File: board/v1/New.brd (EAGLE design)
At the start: 21.8 x 22.6 mm, 28 parts, among them IC2 LTC3525, IC3 MCP1703CB, U3 ATMEGA32U4, X1 USB-MICROB, Y1 16MHz

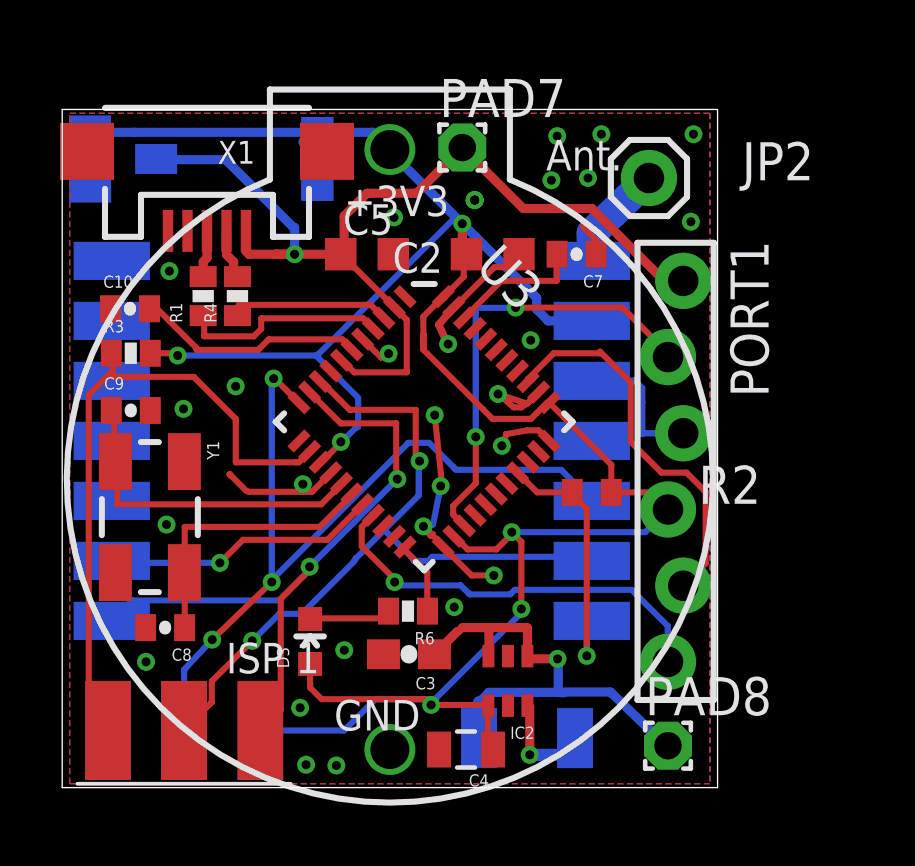
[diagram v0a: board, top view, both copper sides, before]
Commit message: some clearance fix
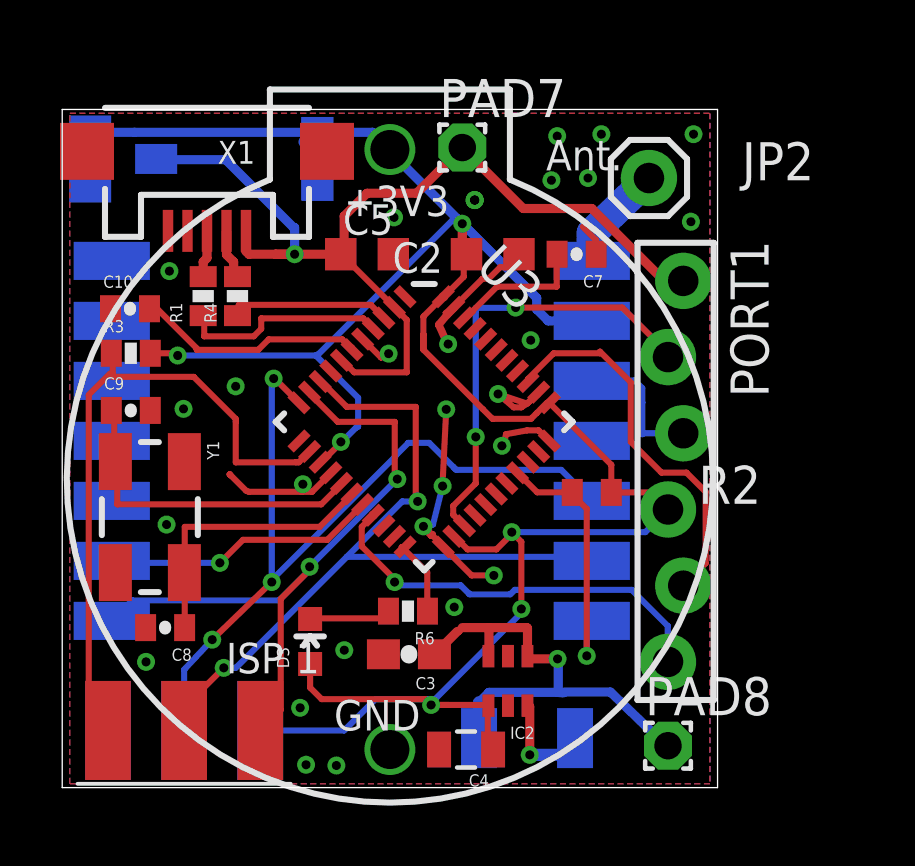
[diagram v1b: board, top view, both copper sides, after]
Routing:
- net SCK: track 25.6 -> 26.7 mm
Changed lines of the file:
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@@
 <autorouter>
 <pass name="Default">
-<param name="RoutingGrid" value="0.05mm"/>
+<param name="RoutingGrid" value="0.1mm"/>
 <param name="tpViaShape" value="round"/>
 <param name="PrefDir.1" value="|"/>
@@
 <wire x1="11.648" y1="14.848" x2="11.640103125" y2="14.848" width="0.2032" layer="1"/>
 <wire x1="11.640103125" y1="14.848" x2="11.0303875" y2="15.457715625" width="0.2032" layer="1"/>
-<via x="13.432" y="12.925" extent="1-16" drill="0.3"/>
+<via x="13.816" y="13.117" extent="1-16" drill="0.3"/>
 <wire x1="18.811" y1="18.288" x2="18.811" y2="18.757" width="0.2032" layer="1"/>
 <wire x1="18.811" y1="18.757" x2="18.368" y2="19.2" width="0.2032" layer="1"/>
 <wire x1="14.070946875" y1="16.518375" x2="14.086375" y2="16.518375" width="0.2032" layer="1"/>
-<wire x1="14.086375" y1="16.518375" x2="15.424" y2="17.856" width="0.2032" layer="1"/>
-<wire x1="15.424" y1="17.856" x2="15.81" y2="17.856" width="0.2032" layer="1"/>
 <wire x1="15.81" y1="17.856" x2="16.242" y2="18.288" width="0.2032" layer="1"/>
 <via x="14.764" y="20.093" extent="1-16" drill="0.3"/>
@@
 <wire x1="15.403" y1="7.581" x2="14.6644625" y2="7.581" width="0.2032" layer="1"/>
 <wire x1="14.6644625" y1="7.581" x2="13.71739375" y2="8.52806875" width="0.2032" layer="1"/>
-<wire x1="13.432" y1="12.925" x2="13.688" y2="10.504" width="0.2032" layer="1"/>
-<wire x1="13.688" y1="10.504" x2="13.632" y2="10.56" width="0.2032" layer="1"/>
-<via x="13.632" y="10.56" extent="1-16" drill="0.3"/>
-<wire x1="13.632" y1="10.56" x2="13.376" y2="9.28" width="0.2032" layer="16"/>
+<wire x1="13.816" y1="13.117" x2="13.688" y2="10.504" width="0.2032" layer="1"/>
+<wire x1="13.688" y1="10.504" x2="13.696" y2="10.56" width="0.2032" layer="1"/>
+<via x="13.696" y="10.56" extent="1-16" drill="0.3"/>
+<wire x1="13.696" y1="10.56" x2="13.376" y2="9.28" width="0.2032" layer="16"/>
 <wire x1="13.376" y1="9.28" x2="13.056" y2="9.216" width="0.2032" layer="16"/>
 <via x="13.056" y="9.216" extent="1-16" drill="0.3"/>
@@
 <wire x1="6.65" y1="10.9" x2="6.599" y2="10.951" width="0.2032" layer="1"/>
 <wire x1="7.15" y1="10.4" x2="7.243" y2="10.368" width="0.2032" layer="1"/>
+<wire x1="14.070946875" y1="16.518375" x2="15.024571875" y2="17.472" width="0.2032" layer="1"/>
+<wire x1="15.024571875" y1="17.472" x2="15.232" y2="17.472" width="0.2032" layer="1"/>
+<wire x1="15.232" y1="17.472" x2="15.616" y2="17.856" width="0.2032" layer="1"/>
+<wire x1="15.616" y1="17.856" x2="15.81" y2="17.856" width="0.2032" layer="1"/>
 </signal>
 <signal name="SCK">
@@
 <contactref element="U$2" pad="SCK"/>
 <contactref element="U3" pad="9"/>
-<wire x1="13.248" y1="8.065" x2="12.736" y2="8.065" width="0.2032" layer="16"/>
 <wire x1="9.616175" y1="14.0435" x2="9.6365" y2="14.0435" width="0.2032" layer="1"/>
-<via x="12.928" y="11.392" extent="1-16" drill="0.3"/>
-<wire x1="12.9" y1="11.35" x2="12.928" y2="11.392" width="0.2032" layer="16"/>
 <wire x1="18.55" y1="8.2" x2="18.65" y2="8.1" width="0.2032" layer="16"/>
-<wire x1="13.35" y1="8.2" x2="18.55" y2="8.2" width="0.2032" layer="16"/>
-<wire x1="13.3" y1="8.15" x2="13.35" y2="8.2" width="0.2032" layer="16"/>
 <wire x1="18.65" y1="8.1" x2="18.668" y2="8.065" width="0.2032" layer="16"/>
-<wire x1="13.3" y1="8.15" x2="13.248" y2="8.065" width="0.2032" layer="16"/>
-<wire x1="12.9" y1="10.25" x2="12.9" y2="11.25" width="0.2032" layer="16"/>
-<wire x1="10.8" y1="8.15" x2="11.75" y2="9.1" width="0.2032" layer="16"/>
-<wire x1="11.75" y1="9.1" x2="12.9" y2="10.25" width="0.2032" layer="16"/>
-<wire x1="12.9" y1="11.25" x2="12.928" y2="11.392" width="0.2032" layer="16"/>
-<wire x1="10.8" y1="8.15" x2="10.753" y2="8.065" width="0.2032" layer="16"/>
-<wire x1="12.7" y1="8.15" x2="11.8" y2="9.05" width="0.2032" layer="16"/>
-<wire x1="11.8" y1="9.05" x2="11.75" y2="9.1" width="0.2032" layer="16"/>
-<wire x1="12.7" y1="8.15" x2="12.736" y2="8.065" width="0.2032" layer="16"/>
-<wire x1="10.6" y1="13.1" x2="9.7" y2="14" width="0.2032" layer="1"/>
-<wire x1="12.8" y1="13.1" x2="10.6" y2="13.1" width="0.2032" layer="1"/>
-<wire x1="12.8" y1="11.5" x2="12.8" y2="13.1" width="0.2032" layer="1"/>
-<wire x1="12.9" y1="11.4" x2="12.8" y2="11.5" width="0.2032" layer="1"/>
+<wire x1="5.1" y1="2.45" x2="5.08" y2="2.413" width="0.2032" layer="1"/>
+<wire x1="5.1" y1="2.5" x2="5.08" y2="2.413" width="0.2032" layer="1"/>
+<wire x1="10.5" y1="8.2" x2="18.5" y2="8.2" width="0.2032" layer="16"/>
+<wire x1="6.8" y1="4.5" x2="10.5" y2="8.2" width="0.2032" layer="16"/>
+<wire x1="6.4" y1="4.5" x2="6.8" y2="4.5" width="0.2032" layer="16"/>
+<wire x1="5.1" y1="3.2" x2="6.4" y2="4.5" width="0.2032" layer="1"/>
+<wire x1="5.1" y1="2.6" x2="5.1" y2="3.2" width="0.2032" layer="1"/>
+<wire x1="18.5" y1="8.2" x2="18.668" y2="8.065" width="0.2032" layer="16"/>
+<wire x1="5.1" y1="2.6" x2="5.08" y2="2.413" width="0.2032" layer="1"/>
+<via x="6.4" y="4.5" extent="1-16" drill="0.3"/>
+<wire x1="10.5" y1="8.2" x2="12.348" y2="10.048" width="0.2032" layer="16"/>
+<wire x1="12.348" y1="10.048" x2="12.864" y2="10.048" width="0.2032" layer="16"/>
+<via x="12.864" y="10.048" extent="1-16" drill="0.3"/>
+<wire x1="9.6" y1="14.1" x2="9.616175" y2="14.0435" width="0.2032" layer="1"/>
+<wire x1="9.6" y1="14.1" x2="9.6" y2="14.08" width="0.2032" layer="1"/>
+<wire x1="10.5" y1="13.2" x2="9.7" y2="14" width="0.2032" layer="1"/>
+<wire x1="12.8" y1="13.2" x2="10.5" y2="13.2" width="0.2032" layer="1"/>
+<wire x1="12.8" y1="10.1" x2="12.8" y2="13.2" width="0.2032" layer="1"/>
 <wire x1="9.7" y1="14" x2="9.616175" y2="14.0435" width="0.2032" layer="1"/>
-<wire x1="12.9" y1="11.4" x2="12.928" y2="11.392" width="0.2032" layer="1"/>
-<wire x1="6" y1="3.35" x2="5.1" y2="2.45" width="0.2032" layer="1"/>
-<wire x1="6" y1="4.05" x2="6" y2="3.35" width="0.2032" layer="1"/>
-<wire x1="7.35" y1="5.4" x2="6" y2="4.05" width="0.2032" layer="1"/>
-<wire x1="8.25" y1="6.3" x2="7.35" y2="5.4" width="0.2032" layer="16"/>
-<wire x1="9" y1="6.3" x2="8.25" y2="6.3" width="0.2032" layer="16"/>
-<wire x1="10.7" y1="8" x2="9" y2="6.3" width="0.2032" layer="16"/>
-<wire x1="5.1" y1="2.45" x2="5.08" y2="2.413" width="0.2032" layer="1"/>
-<wire x1="10.7" y1="8" x2="10.753" y2="8.065" width="0.2032" layer="16"/>
-<via x="7.35" y="5.4" extent="1-16" drill="0.3"/>
+<wire x1="12.8" y1="10.1" x2="12.864" y2="10.048" width="0.2032" layer="1"/>
 </signal>
 <signal name="MOSI">
@@
 <wire x1="7.65" y1="2.45" x2="7.62" y2="2.413" width="0.2032" layer="1"/>
 <wire x1="9.25" y1="7.85" x2="9.264" y2="7.871" width="0.2032" layer="1"/>
-<wire x1="10.3" y1="12.65" x2="9.3" y2="13.65" width="0.2032" layer="1"/>
-<wire x1="12.15" y1="12.65" x2="10.3" y2="12.65" width="0.2032" layer="1"/>
-<wire x1="12.15" y1="10.8" x2="12.15" y2="12.65" width="0.2032" layer="1"/>
 <wire x1="9.3" y1="13.65" x2="9.262621875" y2="13.689946875" width="0.2032" layer="1"/>
-<wire x1="12.15" y1="10.8" x2="12.185" y2="10.792" width="0.2032" layer="1"/>
+<wire x1="10.2" y1="12.7" x2="9.3" y2="13.6" width="0.2032" layer="1"/>
+<wire x1="12.1" y1="12.7" x2="10.2" y2="12.7" width="0.2032" layer="1"/>
+<wire x1="12.1" y1="10.8" x2="12.1" y2="12.7" width="0.2032" layer="1"/>
+<wire x1="9.3" y1="13.6" x2="9.262621875" y2="13.689946875" width="0.2032" layer="1"/>
+<wire x1="12.1" y1="10.8" x2="12.185" y2="10.792" width="0.2032" layer="1"/>
 </signal>
 <signal name="N$3">
@@
 <contactref element="C7" pad="2"/>
 <contactref element="U3" pad="42"/>
-<wire x1="15.65" y1="17.4" x2="14.45" y2="16.2" width="0.2032" layer="1"/>
-<wire x1="17.5" y1="17.4" x2="15.65" y2="17.4" width="0.2032" layer="1"/>
-<wire x1="17.5" y1="18.25" x2="17.5" y2="17.4" width="0.2032" layer="1"/>
 <wire x1="14.45" y1="16.2" x2="14.4245" y2="16.164821875" width="0.2032" layer="1"/>
 <wire x1="17.5" y1="18.25" x2="17.511" y2="18.288" width="0.2032" layer="1"/>
+<wire x1="15.508" y1="17.208" x2="14.5" y2="16.2" width="0.2032" layer="1"/>
+<wire x1="17.5" y1="17.208" x2="15.508" y2="17.208" width="0.2032" layer="1"/>
+<wire x1="17.5" y1="18.2" x2="17.5" y2="17.208" width="0.2032" layer="1"/>
+<wire x1="14.5" y1="16.2" x2="14.4245" y2="16.164821875" width="0.2032" layer="1"/>
+<wire x1="17.5" y1="18.2" x2="17.511" y2="18.288" width="0.2032" layer="1"/>
 </signal>
 <signal name="TXO">

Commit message: PCB revision after the MISO/MOSI pins were messed up
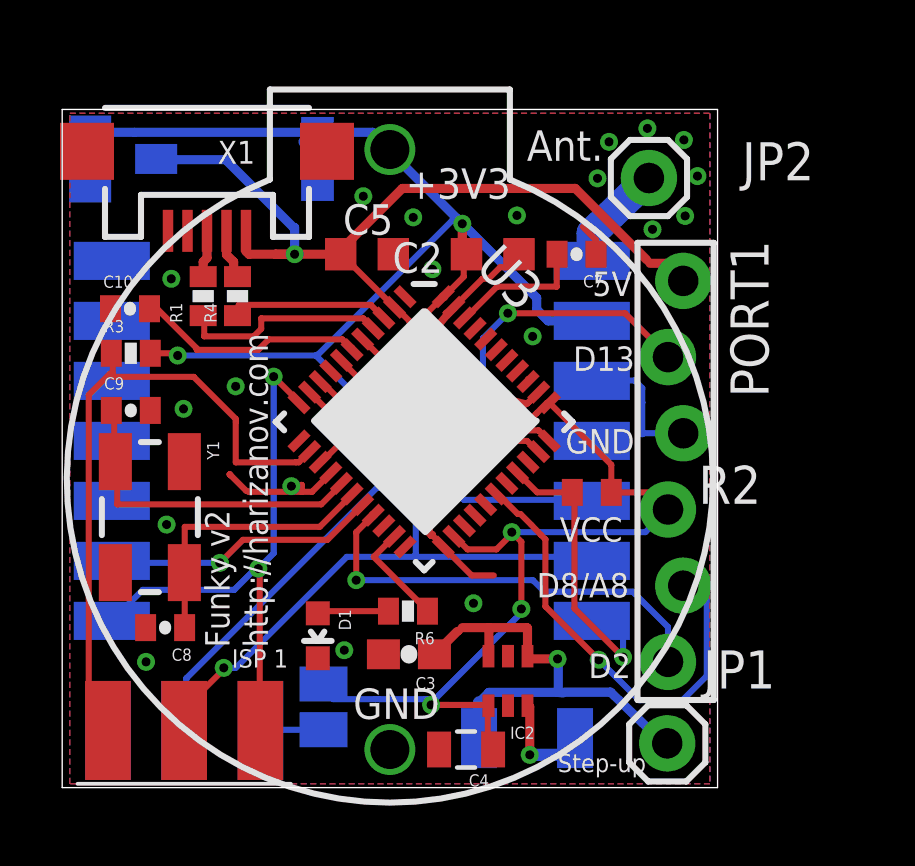
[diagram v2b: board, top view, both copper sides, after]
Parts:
- removed D3: Green, SparkFun:LED-0603
- removed PAD7, PAD8: WIREPAD1,6/0,9, wirepad:1,6/0,9
- added D1: Green, SparkFun:LED-0603
- added JP1: M01PTH, SparkFun:1X01
- added SJ1: (no value), jumper:SJ
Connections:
- net D17 renamed RXLED
- removed net TXLED: R6.1, U3.22
- new net N$8: U3.22
- new net N$9: SJ1.1, U$2.VCC
- net A0: no longer PORT1.5
- net D13: now also PORT1.2
- net D4: no longer PORT1.2
- net D8: now also PORT1.5
- net GND: now also D1.C
- net MISO: now also U$1.SDO, U$2.MISO; no longer U$1.SDI, U$2.MOSI
- net MOSI: now also U$1.SDI, U$2.MOSI; no longer U$1.SDO, U$2.MISO
- net N$6: now also D1.A; no longer D3.C
- net TXO: now also R6.1
- net VBUS: no longer PAD7.1
- net VCC: now also SJ1.2; no longer D3.A, U$2.VCC
- net VIN: now also JP1.1; no longer PAD8.1
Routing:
- net D8: track 0.00 -> 15.3 mm, vias 0 -> 1
- net D4: track 15.1 -> 0.12 mm, vias 2 -> 0
- net D13: track 0.00 -> 13.0 mm, vias 0 -> 2
- net A0: track 12.9 -> 0.09 mm
- net MISO: track 27.7 -> 19.0 mm, vias 3 -> 2
- net VCC: track 86.7 -> 79.7 mm
- net TXO: track 0.00 -> 3.67 mm
- net GND: track 30.6 -> 27.5 mm, vias 29 -> 24
- net TXLED: track 2.78 -> 0.00 mm
- net SCK: track 26.7 -> 24.5 mm
- net N$9: track 0.00 -> 2.12 mm
- net D10: track 9.06 -> 10.5 mm
- net MOSI: track 23.0 -> 24.3 mm, vias 2 -> 1
- net D2: track 14.1 -> 14.7 mm
- net VBUS: track 33.9 -> 33.3 mm
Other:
- board text added: "5V"
- board text added: "D13"
- board text added: "D2"
- board text added: "D8/A8"
- board text added: "Funky v2"
- board text added: "Step-up"
- board text added: "VCC"
- board text added: "http://harizanov.com"
